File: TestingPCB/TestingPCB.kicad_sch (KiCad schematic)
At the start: 15 parts, among them J1 Conn_01x04, J2 USB_C_Receptacle_USB2.0_14P, J3 Conn_01x08, U1 SC0915, U2 CP2102N-Axx-xQFN24, U3 USBLC6-2P6

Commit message: v1 of PCB
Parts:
- added H1, H2, H3, H4: MountingHole, MountingHole:MountingHole_3.2mm_M3_ISO7380_Pad_TopBottom, symbol Mechanical:MountingHole
- J2: Manufacturer Part Number 2171790001 -> USB4105-GF-A

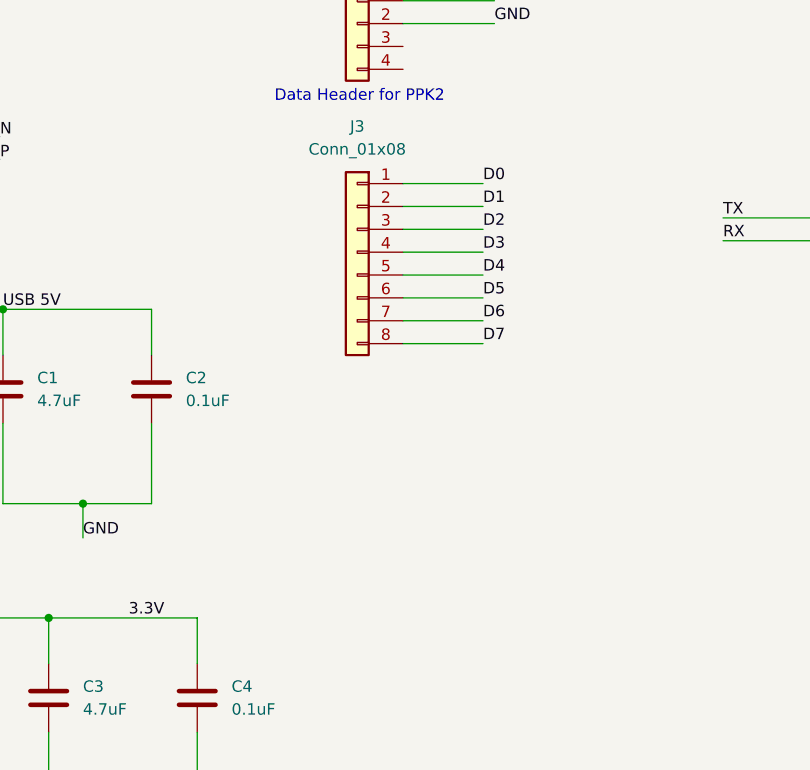
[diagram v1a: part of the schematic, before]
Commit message: Started swapping to 10 pin logic connector
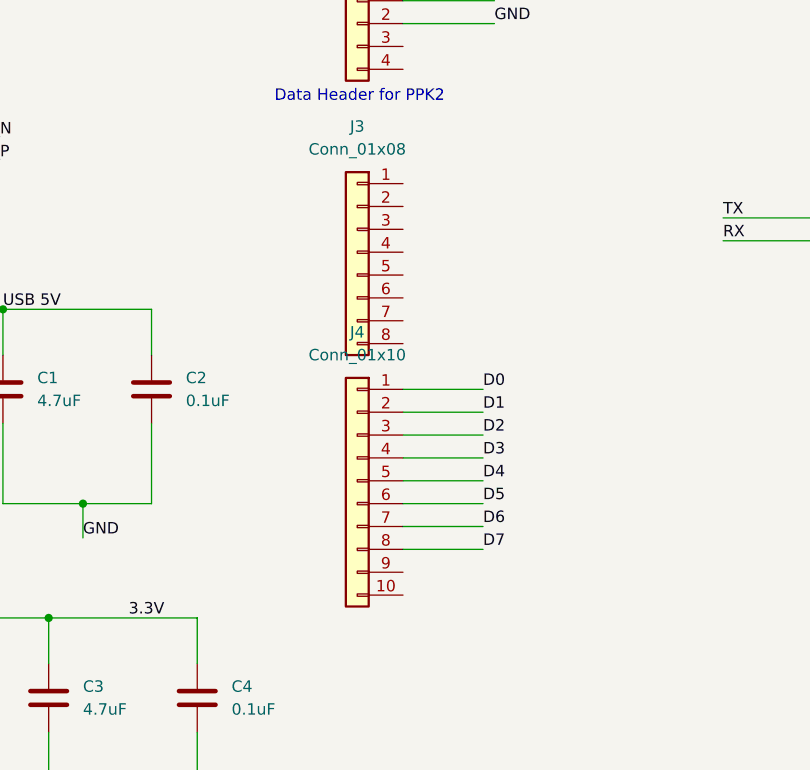
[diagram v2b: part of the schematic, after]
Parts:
- added J4: Conn_01x10, Connector_Harwin:Harwin_M20-89010xx_1x10_P2.54mm_Horizontal, symbol Connector_Generic:Conn_01x10
- J3: Manufacturer Part Number M20-8900805 -> M20-8891045
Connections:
- net D0: now also J4.1 (Pin_1); no longer J3.1 (Pin_1)
- net D1: now also J4.2 (Pin_2); no longer J3.2 (Pin_2)
- net D2: now also J4.3 (Pin_3); no longer J3.3 (Pin_3)
- net D3: now also J4.4 (Pin_4); no longer J3.4 (Pin_4)
- net D4: now also J4.5 (Pin_5); no longer J3.5 (Pin_5)
- net D5: now also J4.6 (Pin_6); no longer J3.6 (Pin_6)
- net D6: now also J4.7 (Pin_7); no longer J3.7 (Pin_7)
- net D7: now also J4.8 (Pin_8); no longer J3.8 (Pin_8)
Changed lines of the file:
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@@
-	(wire
-		(pts
-			(xy 154.94 48.26) (xy 163.83 48.26)
-		)
-		(stroke
-			(width 0)
-			(type default)
-		)
-	)
 	(wire
 		(pts
@@
 	(wire
 		(pts
+			(xy 154.94 86.36) (xy 163.83 86.36)
+		)
+		(stroke
+			(width 0)
+			(type default)
+		)
+	)
+	(wire
+		(pts
 			(xy 97.79 40.64) (xy 107.95 40.64)
 		)
@@
 	(wire
 		(pts
-			(xy 154.94 60.96) (xy 163.83 60.96)
-		)
-		(stroke
-			(width 0)
-			(type default)
-		)
-	)
-	(wire
-		(pts
 			(xy 83.82 160.02) (xy 83.82 165.1)
 		)
@@
 	(wire
 		(pts
+			(xy 154.94 73.66) (xy 163.83 73.66)
+		)
+		(stroke
+			(width 0)
+			(type default)
+		)
+	)
+	(wire
+		(pts
 			(xy 259.08 118.11) (xy 264.16 118.11)
 		)
@@
 	(wire
 		(pts
-			(xy 154.94 63.5) (xy 163.83 63.5)
-		)
-		(stroke
-			(width 0)
-			(type default)
-		)
-	)
-	(wire
-		(pts
 			(xy 85.09 93.98) (xy 85.09 100.33)
 		)
@@
 	(wire
 		(pts
-			(xy 154.94 45.72) (xy 163.83 45.72)
-		)
-		(stroke
-			(width 0)
-			(type default)
-		)
-	)
-	(wire
-		(pts
 			(xy 115.57 93.98) (xy 115.57 99.06)
 		)
@@
 	(wire
 		(pts
+			(xy 154.94 81.28) (xy 163.83 81.28)
+		)
+		(stroke
+			(width 0)
+			(type default)
+		)
+	)
+	(wire
+		(pts
 			(xy 66.04 127) (xy 71.12 127)
 		)
@@
 	(wire
 		(pts
+			(xy 154.94 71.12) (xy 163.83 71.12)
+		)
+		(stroke
+			(width 0)
+			(type default)
+		)
+	)
+	(wire
+		(pts
 			(xy 46.99 38.1) (xy 53.34 38.1)
 		)
@@
 	(wire
 		(pts
-			(xy 154.94 50.8) (xy 163.83 50.8)
-		)
-		(stroke
-			(width 0)
-			(type default)
-		)
-	)
-	(wire
-		(pts
 			(xy 53.34 44.45) (xy 53.34 45.72)
 		)
@@
 	(wire
 		(pts
+			(xy 154.94 78.74) (xy 163.83 78.74)
+		)
+		(stroke
+			(width 0)
+			(type default)
+		)
+	)
+	(wire
+		(pts
 			(xy 115.57 106.68) (xy 115.57 115.57)
 		)
@@
 	(wire
 		(pts
-			(xy 154.94 55.88) (xy 163.83 55.88)
-		)
-		(stroke
-			(width 0)
-			(type default)
-		)
-	)
-	(wire
-		(pts
 			(xy 66.04 87.63) (xy 66.04 95.25)
 		)
@@
 	(wire
 		(pts
+			(xy 154.94 83.82) (xy 163.83 83.82)
+		)
+		(stroke
+			(width 0)
+			(type default)
+		)
+	)
+	(wire
+		(pts
 			(xy 259.08 120.65) (xy 259.08 118.11)
 		)
@@
 	(wire
 		(pts
+			(xy 154.94 68.58) (xy 163.83 68.58)
+		)
+		(stroke
+			(width 0)
+			(type default)
+		)
+	)
+	(wire
+		(pts
 			(xy 50.8 121.92) (xy 71.12 121.92)
 		)
@@
 	(wire
 		(pts
-			(xy 154.94 58.42) (xy 163.83 58.42)
-		)
-		(stroke
-			(width 0)
-			(type default)
-		)
-	)
-	(wire
-		(pts
 			(xy 132.08 93.98) (xy 132.08 99.06)
 		)
@@
 	(wire
 		(pts
-			(xy 154.94 53.34) (xy 163.83 53.34)
-		)
-		(stroke
-			(width 0)
-			(type default)
-		)
-	)
-	(wire
-		(pts
 			(xy 74.93 40.64) (xy 87.63 40.64)
 		)
@@
 		(pts
 			(xy 46.99 43.18) (xy 53.34 43.18)
+		)
+		(stroke
+			(width 0)
+			(type default)
+		)
+	)
+	(wire
+		(pts
+			(xy 154.94 76.2) (xy 163.83 76.2)
 		)
 		(stroke
@@
 		)
 	)
-	(label "D1"
-		(at 163.83 48.26 0)
-		(effects
-			(font
-				(size 1.27 1.27)
-			)
-			(justify left bottom)
-		)
-	)
 	(label "D_P"
 		(at 66.04 127 0)
@@
 		)
 	)
+	(label "D3"
+		(at 163.83 76.2 0)
+		(effects
+			(font
+				(size 1.27 1.27)
+			)
+			(justify left bottom)
+		)
+	)
 	(label "3.3V"
 		(at 124.46 93.98 0)
@@
 		)
 	)
+	(label "D1"
+		(at 163.83 71.12 0)
+		(effects
+			(font
+				(size 1.27 1.27)
+			)
+			(justify left bottom)
+		)
+	)
 	(label "GND"
 		(at 165.1 27.94 0)
@@
 	)
 	(label "D2"
-		(at 163.83 50.8 0)
+		(at 163.83 73.66 0)
 		(effects
 			(font
@@
 		)
 	)
+	(label "D6"
+		(at 163.83 83.82 0)
+		(effects
+			(font
+				(size 1.27 1.27)
+			)
+			(justify left bottom)
+		)
+	)
 	(label "GND"
 		(at 264.16 118.11 0)
@@
 		)
 	)
+	(label "D4"
+		(at 163.83 78.74 0)
+		(effects
+			(font
+				(size 1.27 1.27)
+			)
+			(justify left bottom)
+		)
+	)
 	(label "USB 5V"
 		(at 53.34 25.4 0)
@@
 		)
 	)
-	(label "D4"
-		(at 163.83 55.88 0)
+	(label "D0"
+		(at 163.83 68.58 0)
 		(effects
 			(font
@@
 		)
 	)
-	(label "D6"
-		(at 163.83 60.96 0)
-		(effects
-			(font
-				(size 1.27 1.27)
-			)
-			(justify left bottom)
-		)
-	)
 	(label "RX"
 		(at 190.5 52.07 0)
@@
 		)
 	)
-	(label "D0"
-		(at 163.83 45.72 0)
+	(label "D7"
+		(at 163.83 86.36 0)
 		(effects
 			(font
@@
 		)
 	)
-	(label "D5"
-		(at 163.83 58.42 0)
-		(effects
-			(font
-				(size 1.27 1.27)
-			)
-			(justify left bottom)
-		)
-	)
 	(label "GND"
 		(at 92.71 52.07 0)
@@
 		)
 	)
-	(label "D3"
-		(at 163.83 53.34 0)
-		(effects
-			(font
-				(size 1.27 1.27)
-			)
-			(justify left bottom)
-		)
-	)
-	(label "D7"
-		(at 163.83 63.5 0)
+	(label "D5"
+		(at 163.83 81.28 0)
 		(effects
 			(font
@@
 			)
 		)
-		(property "Manufacturer Part Number" "M20-8900805"
+		(property "Manufacturer Part Number" "M20-8891045"
 			(at 149.86 53.34 0)
 			(effects
@@
 					(unit 1)
 				)
+			)
+		)
+	)
+	(symbol
+		(lib_id "Connector_Generic:Conn_01x10")
+		(at 149.86 78.74 0)
+		(mirror y)
+		(unit 1)
+		(exclude_from_sim no)
+		(in_bom yes)
+		(on_board yes)
+		(dnp no)
+		(fields_autoplaced yes)
+		(property "Reference" "J4"
+			(at 149.86 62.23 0)
+			(effects
+				(font
+					(size 1.27 1.27)
+				)
+			)
+		)
+		(property "Value" "Conn_01x10"
+			(at 149.86 64.77 0)
+			(effects
+				(font
+					(size 1.27 1.27)
+				)
+			)
+		)
+		(property "Footprint" "Connector_Harwin:Harwin_M20-89010xx_1x10_P2.54mm_Horizontal"
+			(at 149.86 78.74 0)
+			(effects
+				(font
+					(size 1.27 1.27)
+				)
+				(hide yes)
+			)
+		)
+		(property "Datasheet" "~"
+			(at 149.86 78.74 0)
+			(effects
+				(font
+					(size 1.27 1.27)
+				)
+				(hide yes)
+			)
+		)
+		(property "Description" "Generic connector, single row, 01x10, script generated (kicad-library-utils/schlib/autogen/connector/)"
+			(at 149.86 78.74 0)
+			(effects
+				(font
+					(size 1.27 1.27)
+				)
+				(hide yes)
+			)
+		)
+		(pin "5"
+		)
+		(pin "8"
+		)
+		(pin "4"
+		)
+		(pin "7"
+		)
+		(pin "1"
+		)
+		(pin "10"
+		)
+		(pin "9"
+		)
+		(pin "3"
+		)
+		(pin "2"
+		)
+		(pin "6"
+		)
+		(instances
+			(project ""
+				(path "/8bb8fabd-08ec-4863-9d8b-dc20b6f396de"
+					(reference "J4")
+					(unit 1)
+				)

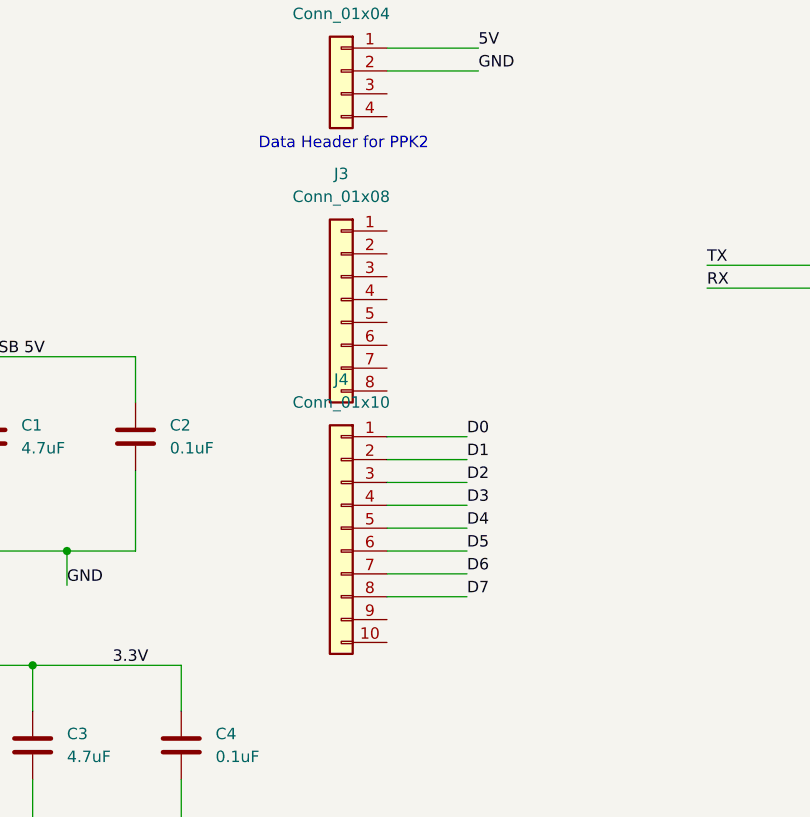
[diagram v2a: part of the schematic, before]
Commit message: Updated PCB with 10 pin logic connector
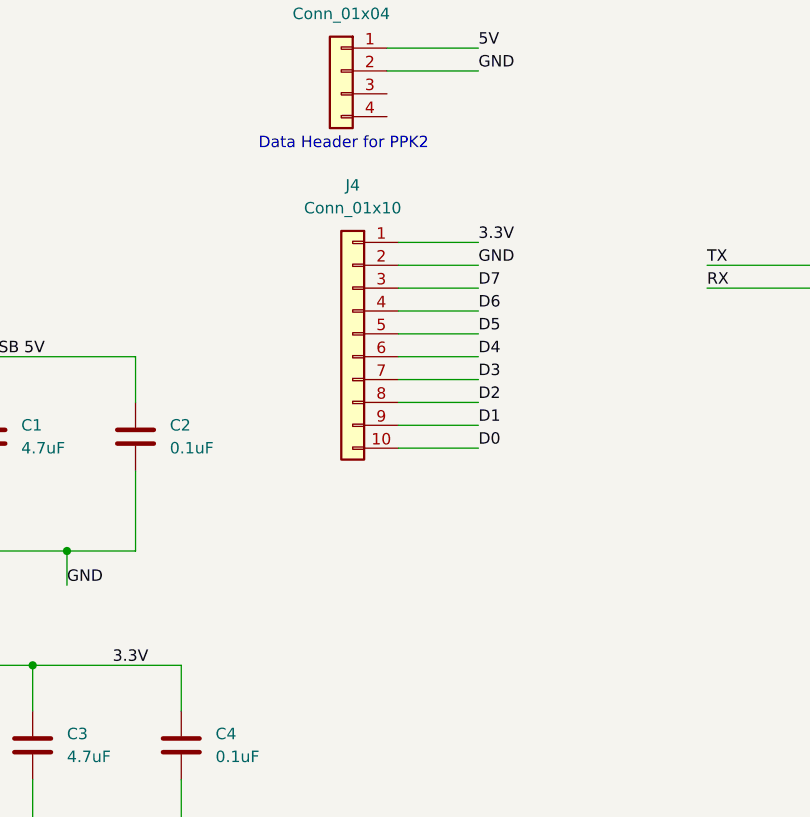
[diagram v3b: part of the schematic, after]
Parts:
- removed J3: Conn_01x08, Connector_Harwin:Harwin_M20-89008xx_1x08_P2.54mm_Horizontal, symbol Connector_Generic:Conn_01x08
- J4: footprint Connector_Harwin:Harwin_M20-89010xx_1x10_P2.54mm_Horizontal -> Footprints:HARWIN_M20-8891045
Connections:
- net 3.3V: now also J4.1 (Pin_1)
- net D0: now also J4.10 (Pin_10); no longer J4.1 (Pin_1)
- net D1: now also J4.9 (Pin_9); no longer J4.2 (Pin_2)
- net D2: now also J4.8 (Pin_8); no longer J4.3 (Pin_3)
- net D3: now also J4.7 (Pin_7); no longer J4.4 (Pin_4)
- net D4: now also J4.6 (Pin_6); no longer J4.5 (Pin_5)
- net D5: now also J4.5 (Pin_5); no longer J4.6 (Pin_6)
- net D6: now also J4.4 (Pin_4); no longer J4.7 (Pin_7)
- net D7: now also J4.3 (Pin_3); no longer J4.8 (Pin_8)
- net GND: now also J4.2 (Pin_2)
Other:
- moved on the sheet: J4
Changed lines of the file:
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@@
 	(title_block
 		(title "Thesis PCB")
-		(date "2025-02-25")
+		(date "2025-03-09")
 		(rev "v1.0")
 		(company "Lafayette College Electrical & Computer Engineering Department")
@@
 	(wire
 		(pts
+			(xy 156.21 54.61) (xy 165.1 54.61)
+		)
+		(stroke
+			(width 0)
+			(type default)
+		)
+	)
+	(wire
+		(pts
 			(xy 110.49 81.28) (xy 119.38 81.28)
 		)
@@
 	(wire
 		(pts
+			(xy 156.21 69.85) (xy 165.1 69.85)
+		)
+		(stroke
+			(width 0)
+			(type default)
+		)
+	)
+	(wire
+		(pts
+			(xy 156.21 52.07) (xy 165.1 52.07)
+		)
+		(stroke
+			(width 0)
+			(type default)
+		)
+	)
+	(wire
+		(pts
 			(xy 254 72.39) (xy 262.89 72.39)
 		)
@@
 	(wire
 		(pts
+			(xy 156.21 49.53) (xy 165.1 49.53)
+		)
+		(stroke
+			(width 0)
+			(type default)
+		)
+	)
+	(wire
+		(pts
 			(xy 57.15 27.94) (xy 62.23 27.94)
 		)
@@
 	(wire
 		(pts
+			(xy 156.21 67.31) (xy 165.1 67.31)
+		)
+		(stroke
+			(width 0)
+			(type default)
+		)
+	)
+	(wire
+		(pts
 			(xy 96.52 109.22) (xy 102.87 109.22)
 		)
@@
 	(wire
 		(pts
-			(xy 154.94 86.36) (xy 163.83 86.36)
-		)
-		(stroke
-			(width 0)
-			(type default)
-		)
-	)
-	(wire
-		(pts
 			(xy 97.79 40.64) (xy 107.95 40.64)
 		)
@@
 	(wire
 		(pts
-			(xy 154.94 73.66) (xy 163.83 73.66)
-		)
-		(stroke
-			(width 0)
-			(type default)
-		)
-	)
-	(wire
-		(pts
 			(xy 259.08 118.11) (xy 264.16 118.11)
 		)
@@
 	(wire
 		(pts
+			(xy 156.21 57.15) (xy 165.1 57.15)
+		)
+		(stroke
+			(width 0)
+			(type default)
+		)
+	)
+	(wire
+		(pts
 			(xy 66.04 102.87) (xy 66.04 109.22)
 		)
@@
 	(wire
 		(pts
-			(xy 154.94 81.28) (xy 163.83 81.28)
-		)
-		(stroke
-			(width 0)
-			(type default)
-		)
-	)
-	(wire
-		(pts
 			(xy 66.04 127) (xy 71.12 127)
 		)
@@
 	(wire
 		(pts
+			(xy 156.21 64.77) (xy 165.1 64.77)
+		)
+		(stroke
+			(width 0)
+			(type default)
+		)
+	)
+	(wire
+		(pts
 			(xy 83.82 100.33) (xy 85.09 100.33)
 		)
@@
 	(wire
 		(pts
+			(xy 156.21 46.99) (xy 165.1 46.99)
+		)
+		(stroke
+			(width 0)
+			(type default)
+		)
+	)
+	(wire
+		(pts
 			(xy 74.93 43.18) (xy 87.63 43.18)
 		)
@@
 	(wire
 		(pts
-			(xy 154.94 71.12) (xy 163.83 71.12)
-		)
-		(stroke
-			(width 0)
-			(type default)
-		)
-	)
-	(wire
-		(pts
 			(xy 46.99 38.1) (xy 53.34 38.1)
 		)
@@
 	(wire
 		(pts
-			(xy 154.94 78.74) (xy 163.83 78.74)
-		)
-		(stroke
-			(width 0)
-			(type default)
-		)
-	)
-	(wire
-		(pts
 			(xy 115.57 106.68) (xy 115.57 115.57)
 		)
@@
 	(wire
 		(pts
-			(xy 154.94 83.82) (xy 163.83 83.82)
-		)
-		(stroke
-			(width 0)
-			(type default)
-		)
-	)
-	(wire
-		(pts
 			(xy 259.08 120.65) (xy 259.08 118.11)
 		)
@@
 	(wire
 		(pts
-			(xy 154.94 68.58) (xy 163.83 68.58)
+			(xy 156.21 59.69) (xy 165.1 59.69)
 		)
 		(stroke
@@
 	(wire
 		(pts
+			(xy 156.21 62.23) (xy 165.1 62.23)
+		)
+		(stroke
+			(width 0)
+			(type default)
+		)
+	)
+	(wire
+		(pts
 			(xy 254 64.77) (xy 262.89 64.77)
 		)
@@
 		(pts
 			(xy 46.99 43.18) (xy 53.34 43.18)
-		)
-		(stroke
-			(width 0)
-			(type default)
-		)
-	)
-	(wire
-		(pts
-			(xy 154.94 76.2) (xy 163.83 76.2)
 		)
 		(stroke
@@
 	)
 	(label "D3"
-		(at 163.83 76.2 0)
+		(at 165.1 62.23 0)
 		(effects
 			(font
@@
 	)
 	(label "D1"
-		(at 163.83 71.12 0)
+		(at 165.1 67.31 0)
 		(effects
 			(font
@@
 	)
 	(label "D2"
-		(at 163.83 73.66 0)
+		(at 165.1 64.77 0)
 		(effects
 			(font
@@
 	)
 	(label "D6"
-		(at 163.83 83.82 0)
+		(at 165.1 54.61 0)
 		(effects
 			(font
@@
 	)
 	(label "D4"
-		(at 163.83 78.74 0)
+		(at 165.1 59.69 0)
 		(effects
 			(font
@@
 	)
 	(label "D0"
-		(at 163.83 68.58 0)
+		(at 165.1 69.85 0)
 		(effects
 			(font
@@
 		)
 	)
+	(label "3.3V"
+		(at 165.1 46.99 0)
+		(effects
+			(font
+				(size 1.27 1.27)
+			)
+			(justify left bottom)
+		)
+	)
 	(label "RX"
 		(at 190.5 52.07 0)
@@
 	)
 	(label "D7"
-		(at 163.83 86.36 0)
+		(at 165.1 52.07 0)
 		(effects
 			(font
@@
 		)
 	)
+	(label "GND"
+		(at 165.1 49.53 0)
+		(effects
+			(font
+				(size 1.27 1.27)
+			)
+			(justify left bottom)
+		)
+	)
 	(label "D2"
 		(at 262.89 62.23 0)
@@
 	)
 	(label "D5"
-		(at 163.83 81.28 0)
+		(at 165.1 57.15 0)
 		(effects
 			(font
@@
 	)
 	(symbol
-		(lib_id "Connector_Generic:Conn_01x08")
-		(at 149.86 53.34 0)
-		(mirror y)
-		(unit 1)
-		(exclude_from_sim no)
-		(in_bom yes)
-		(on_board yes)
-		(dnp no)
-		(fields_autoplaced yes)
-		(property "Reference" "J3"
-			(at 149.86 39.37 0)
-			(effects
-				(font
-					(size 1.27 1.27)
-				)
-			)
-		)
-		(property "Value" "Conn_01x08"
-			(at 149.86 41.91 0)
-			(effects
-				(font
-					(size 1.27 1.27)
-				)
-			)
-		)
-		(property "Footprint" "Connector_Harwin:Harwin_M20-89008xx_1x08_P2.54mm_Horizontal"
-			(at 149.86 53.34 0)
-			(effects
-				(font
-					(size 1.27 1.27)
-				)
-				(hide yes)
-			)
-		)
-		(property "Datasheet" "~"
-			(at 149.86 53.34 0)
-			(effects
-				(font
-					(size 1.27 1.27)
-				)
-				(hide yes)
-			)
-		)
-		(property "Description" "Generic connector, single row, 01x08, script generated (kicad-library-utils/schlib/autogen/connector/)"
-			(at 149.86 53.34 0)
-			(effects
-				(font
-					(size 1.27 1.27)
-				)
-				(hide yes)
-			)
-		)
-		(property "Manufacturer Part Number" "M20-8891045"
-			(at 149.86 53.34 0)
-			(effects
-				(font
-					(size 1.27 1.27)
-				)
-				(hide yes)
-			)
-		)
-		(pin "3"
-		)
-		(pin "5"
-		)
-		(pin "7"
-		)
-		(pin "4"
-		)
-		(pin "8"
-		)
-		(pin "2"
-		)
-		(pin "1"
-		)
-		(pin "6"
-		)
-		(instances
-			(project ""
-				(path "/8bb8fabd-08ec-4863-9d8b-dc20b6f396de"
-					(reference "J3")
-					(unit 1)
-				)
-			)
-		)
-	)
-	(symbol
 		(lib_id "Connector_Generic:Conn_01x10")
-		(at 149.86 78.74 0)
+		(at 151.13 57.15 0)
 		(mirror y)
 		(unit 1)
@@
 		(fields_autoplaced yes)
 		(property "Reference" "J4"
-			(at 149.86 62.23 0)
+			(at 151.13 40.64 0)
 			(effects
 				(font
@@
 		)
 		(property "Value" "Conn_01x10"
-			(at 149.86 64.77 0)
+			(at 151.13 43.18 0)
 			(effects
 				(font
@@
 			)
 		)
-		(property "Footprint" "Connector_Harwin:Harwin_M20-89010xx_1x10_P2.54mm_Horizontal"
-			(at 149.86 78.74 0)
+		(property "Footprint" "Footprints:HARWIN_M20-8891045"
+			(at 151.13 57.15 0)
 			(effects
 				(font
@@
 		)
 		(property "Datasheet" "~"
-			(at 149.86 78.74 0)
+			(at 151.13 57.15 0)
 			(effects
 				(font
@@
 		)
 		(property "Description" "Generic connector, single row, 01x10, script generated (kicad-library-utils/schlib/autogen/connector/)"
-			(at 149.86 78.74 0)
+			(at 151.13 57.15 0)
 			(effects
 				(font
